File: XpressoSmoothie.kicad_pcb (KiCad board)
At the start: 2 copper layers, 99.7 x 99.7 mm, 116 parts, among them J1 HEADER_4, J10 HEADER_3X2, J11 Pwr_in, J12 HEADER_4, J13 HEADER_4, J14 HEADER_3X2, J15 HEADER_4, J16 HEADER_3, J17 HEADER_3, J18 HEADER_3, J19 HEADER_2, J2 HEADER_4, J20 HEADER_2, J21 HEADER_2, J22 HEADER_2, J23 HEADER_3, J24 HEADER_3, J25 HEADER_3, J26 USB, J27 HEADER_4, J3 HEADER_3, J4 HEADER_3X2, J5 HEADER_3X2, J6 LPCXPRESSO_GENERIC_HEADER, J7 HEADER_4, J8 HEADER_4, J9 HEADER_3X2, M1 LOGO_OSHW, M2 LOGO_OSHW, Q1 IRLB 8743, Q2 IRLB 8743, Q3 IRLB 8743, Q4 IRLB 8743, SW1 SW_PUSH, SW2 SW_PUSH, U1 POLOLU_A4988, U10 TC4422A, U11 TC4422A, U12 LM1117-3.3, U2 POLOLU_A4988, U3 POLOLU_A4988, U4 POLOLU_A4988, U5 POLOLU_A4988, U6 CONN_MICROSD, U7 LM7812CT, U8 TC4422A, U9 TC4422A

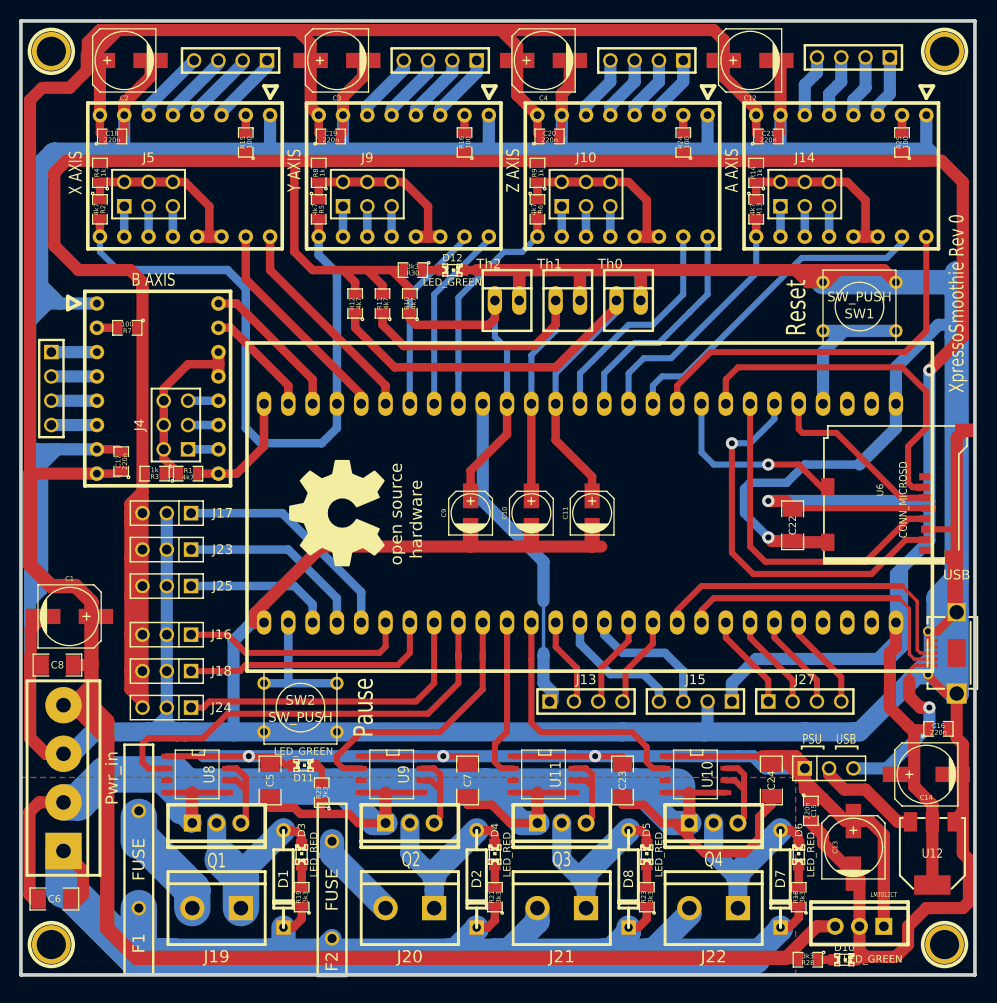
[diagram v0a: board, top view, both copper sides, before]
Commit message: Hid more labels, added some in so that everything is clearly marked and there are no overlaps.
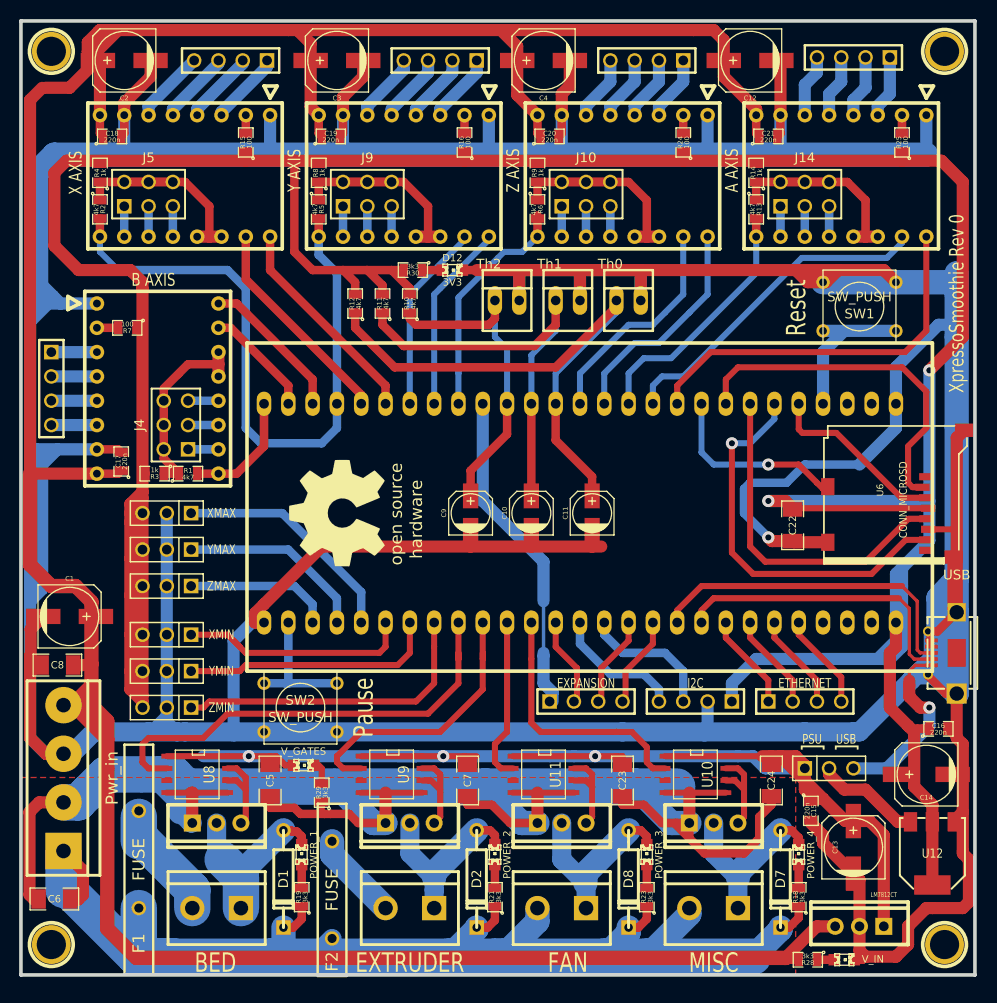
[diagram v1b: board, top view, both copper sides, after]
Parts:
- D10: value LED_GREEN -> V_IN
- D11: value LED_GREEN -> V_GATES
- D12: value LED_GREEN -> 3V3
- D3: value LED_RED -> POWER_1
- D4: value LED_RED -> POWER_2
- D5: value LED_RED -> POWER_3
- D6: value LED_RED -> POWER_4
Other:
- board text added: "BED"
- board text added: "ETHERNET"
- board text added: "EXPANSION"
- board text added: "EXTRUDER"
- board text added: "FAN"
- board text added: "I2C"
- board text added: "MISC"
- board text added: "XMAX"
- board text added: "XMIN"
- board text added: "YMAX"
- board text added: "YMIN"
- board text added: "ZMAX"
- board text added: "ZMIN"
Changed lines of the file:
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@@
     (links 313)
     (no_connects 11)
-    (area 56.388 53.217 179.864657 163.2712)
+    (area 71.564499 53.784499 171.640501 153.860501)
     (thickness 1.6)
-    (drawings 18)
+    (drawings 31)
     (tracks 1095)
     (zones 0)
@@
   )
   (layers
-    (15 F.Cu signal hide)
-    (0 B.Cu signal hide)
+    (15 F.Cu signal)
+    (0 B.Cu signal)
     (16 B.Adhes user)
     (17 F.Adhes user)
     (18 B.Paste user)
     (19 F.Paste user)
-    (20 B.SilkS user hide)
+    (20 B.SilkS user)
     (21 F.SilkS user)
     (22 B.Mask user)
@@
     (descr "Regulateur TO220 serie LM78xx")
     (tags "TR TO220")
-    (fp_text reference Q1 (at 3.937 0 360) (layer F.SilkS)
+    (fp_text reference Q1 (at 3.937 0 360) (layer F.SilkS) hide
       (effects (font (size 1.524 1.016) (thickness 0.2032)))
     )
@@
     (descr "Regulateur TO220 serie LM78xx")
     (tags "TR TO220")
-    (fp_text reference Q2 (at 3.81 -0.127 360) (layer F.SilkS)
+    (fp_text reference Q2 (at 3.81 -0.127 360) (layer F.SilkS) hide
       (effects (font (size 1.524 1.016) (thickness 0.2032)))
     )
@@
     (descr "Regulateur TO220 serie LM78xx")
     (tags "TR TO220")
-    (fp_text reference Q3 (at 3.81 0 360) (layer F.SilkS)
+    (fp_text reference Q3 (at 3.81 0 360) (layer F.SilkS) hide
       (effects (font (size 1.524 1.016) (thickness 0.2032)))
     )
@@
     (descr "Regulateur TO220 serie LM78xx")
     (tags "TR TO220")
-    (fp_text reference Q4 (at 3.81 0 360) (layer F.SilkS)
+    (fp_text reference Q4 (at 3.81 0 360) (layer F.SilkS) hide
       (effects (font (size 1.524 1.016) (thickness 0.2032)))
     )
@@
     (descr "Double rangee de contacts 2 x 5 pins")
     (tags CONN)
-    (fp_text reference J15 (at 0 2.286 180) (layer F.SilkS)
+    (fp_text reference J15 (at 0 2.286 180) (layer F.SilkS) hide
       (effects (font (size 1.016 1.016) (thickness 0.2032)))
     )
@@
     (descr "Connecteur 3 pins")
     (tags "CONN DEV")
-    (fp_text reference J16 (at -5.715 0 180) (layer F.SilkS)
+    (fp_text reference J16 (at -5.715 0 180) (layer F.SilkS) hide
       (effects (font (size 1.016 1.016) (thickness 0.1524)))
     )
@@
     (descr "Connecteur 3 pins")
     (tags "CONN DEV")
-    (fp_text reference J17 (at -5.842 0 180) (layer F.SilkS)
+    (fp_text reference J17 (at -5.842 0 180) (layer F.SilkS) hide
       (effects (font (size 1.016 1.016) (thickness 0.1524)))
     )
@@
     (descr "Connecteur 3 pins")
     (tags "CONN DEV")
-    (fp_text reference J18 (at -5.715 0 180) (layer F.SilkS)
+    (fp_text reference J18 (at -5.715 0 180) (layer F.SilkS) hide
       (effects (font (size 1.016 1.016) (thickness 0.1524)))
     )
@@
     (descr "Connecteur 3 pins")
     (tags "CONN DEV")
-    (fp_text reference J23 (at -5.842 0 180) (layer F.SilkS)
+    (fp_text reference J23 (at -5.842 0 180) (layer F.SilkS) hide
       (effects (font (size 1.016 1.016) (thickness 0.1524)))
     )
@@
     (descr "Connecteur 3 pins")
     (tags "CONN DEV")
-    (fp_text reference J24 (at -5.715 0 180) (layer F.SilkS)
+    (fp_text reference J24 (at -5.715 0 180) (layer F.SilkS) hide
       (effects (font (size 1.016 1.016) (thickness 0.1524)))
     )
@@
     (descr "Connecteur 3 pins")
     (tags "CONN DEV")
-    (fp_text reference J25 (at -5.842 0 180) (layer F.SilkS)
+    (fp_text reference J25 (at -5.842 0 180) (layer F.SilkS) hide
       (effects (font (size 1.016 1.016) (thickness 0.1524)))
     )
@@
     (tags "LED 0805 SMD")
     (attr smd)
-    (fp_text reference D6 (at 2.5654 0.0254 90) (layer F.SilkS)
+    (fp_text reference D6 (at 2.5654 0.0254 90) (layer F.SilkS) hide
       (effects (font (size 0.762 0.762) (thickness 0.127)))
     )
-    (fp_text value LED_RED (at 0 1.27 90) (layer F.SilkS)
+    (fp_text value POWER_4 (at 0 1.27 90) (layer F.SilkS)
       (effects (font (size 0.762 0.762) (thickness 0.127)))
     )
@@
     (tags "LED 0805 SMD")
     (attr smd)
-    (fp_text reference D5 (at 2.6162 -0.0254 90) (layer F.SilkS)
+    (fp_text reference D5 (at 2.6162 -0.0254 90) (layer F.SilkS) hide
       (effects (font (size 0.762 0.762) (thickness 0.127)))
     )
-    (fp_text value LED_RED (at 0 1.27 90) (layer F.SilkS)
+    (fp_text value POWER_3 (at 0 1.27 90) (layer F.SilkS)
       (effects (font (size 0.762 0.762) (thickness 0.127)))
     )
@@
     (tags "LED 0805 SMD")
     (attr smd)
-    (fp_text reference D3 (at 2.5654 0 90) (layer F.SilkS)
+    (fp_text reference D3 (at 2.5654 0 90) (layer F.SilkS) hide
       (effects (font (size 0.762 0.762) (thickness 0.127)))
     )
-    (fp_text value LED_RED (at 0 1.27 90) (layer F.SilkS)
+    (fp_text value POWER_1 (at 0 1.27 90) (layer F.SilkS)
       (effects (font (size 0.762 0.762) (thickness 0.127)))
     )
@@
     (tags "LED 0805 SMD")
     (attr smd)
-    (fp_text reference D4 (at 2.5654 0 90) (layer F.SilkS)
+    (fp_text reference D4 (at 2.5654 0 90) (layer F.SilkS) hide
       (effects (font (size 0.762 0.762) (thickness 0.127)))
     )
-    (fp_text value LED_RED (at 0 1.27 90) (layer F.SilkS)
+    (fp_text value POWER_2 (at 0 1.27 90) (layer F.SilkS)
       (effects (font (size 0.762 0.762) (thickness 0.127)))
     )
@@
     (descr "Bornier d'alimentation 2 pins")
     (tags DEV)
-    (fp_text reference J22 (at 0 -5.08 180) (layer F.SilkS)
+    (fp_text reference J22 (at 0 -5.08 180) (layer F.SilkS) hide
       (effects (font (thickness 0.3048)))
     )
@@
     (descr "Bornier d'alimentation 2 pins")
     (tags DEV)
-    (fp_text reference J19 (at 0 -5.08 180) (layer F.SilkS)
+    (fp_text reference J19 (at 0 -5.08 180) (layer F.SilkS) hide
       (effects (font (thickness 0.3048)))
     )
@@
     (descr "Bornier d'alimentation 2 pins")
     (tags DEV)
-    (fp_text reference J20 (at 0 -5.08 180) (layer F.SilkS)
+    (fp_text reference J20 (at 0 -5.08 180) (layer F.SilkS) hide
       (effects (font (thickness 0.3048)))
     )
@@
     (descr "Bornier d'alimentation 2 pins")
     (tags DEV)
-    (fp_text reference J21 (at 0 -5.08 180) (layer F.SilkS)
+    (fp_text reference J21 (at 0 -5.08 180) (layer F.SilkS) hide
       (effects (font (thickness 0.3048)))
     )
@@
     (tags "LED 0805 SMD")
     (attr smd)
-    (fp_text reference D10 (at 0 -1.27) (layer F.SilkS)
+    (fp_text reference D10 (at 0 -1.27) (layer F.SilkS) hide
       (effects (font (size 0.762 0.762) (thickness 0.127)))
     )
-    (fp_text value LED_GREEN (at 2.9845 -0.0635) (layer F.SilkS)
+    (fp_text value V_IN (at 2.9845 -0.0635) (layer F.SilkS)
       (effects (font (size 0.762 0.762) (thickness 0.127)))
     )
@@
     (tags "LED 0805 SMD")
     (attr smd)
-    (fp_text reference D11 (at 0 1.3335) (layer F.SilkS)
+    (fp_text reference D11 (at 0 1.3335) (layer F.SilkS) hide
       (effects (font (size 0.762 0.762) (thickness 0.127)))
     )
-    (fp_text value LED_GREEN (at 0 -1.4605) (layer F.SilkS)
+    (fp_text value V_GATES (at 0 -1.4605) (layer F.SilkS)
       (effects (font (size 0.762 0.762) (thickness 0.127)))
     )
@@
       (effects (font (size 0.762 0.762) (thickness 0.127)))
     )
-    (fp_text value LED_GREEN (at 0 1.27) (layer F.SilkS)
+    (fp_text value 3V3 (at 0 1.27) (layer F.SilkS)
       (effects (font (size 0.762 0.762) (thickness 0.127)))
     )
@@
     (descr "Double rangee de contacts 2 x 5 pins")
     (tags CONN)
-    (fp_text reference J13 (at 0 -2.286) (layer F.SilkS)
+    (fp_text reference J13 (at 0 -2.286) (layer F.SilkS) hide
       (effects (font (size 1.016 1.016) (thickness 0.2032)))
     )
@@
     (descr "Double rangee de contacts 2 x 5 pins")
     (tags CONN)
-    (fp_text reference J27 (at 0 -2.286) (layer F.SilkS)
+    (fp_text reference J27 (at 0 -2.286) (layer F.SilkS) hide
       (effects (font (size 1.016 1.016) (thickness 0.2032)))
     )
@@
       (xy -3.37312 4.99872)) (layer F.SilkS) (width 0.00254))
   )
+  (gr_text MISC (at 144.145 152.4) (layer F.SilkS)
+    (effects (font (size 2.032 1.524) (thickness 0.3048)))
+  )
+  (gr_text FAN (at 128.905 152.4) (layer F.SilkS)
+    (effects (font (size 2.032 1.524) (thickness 0.3048)))
+  )
+  (gr_text EXTRUDER (at 112.395 152.4) (layer F.SilkS)
+    (effects (font (size 2.032 1.524) (thickness 0.3048)))
+  )
+  (gr_text BED (at 92.075 152.4) (layer F.SilkS)
+    (effects (font (size 2.032 1.524) (thickness 0.3048)))
+  )
+  (gr_text ETHERNET (at 153.67 123.19) (layer F.SilkS)
+    (effects (font (size 1.016 0.762) (thickness 0.1524)))
+  )
+  (gr_text I2C (at 142.24 123.19) (layer F.SilkS)
+    (effects (font (size 1.016 0.762) (thickness 0.1524)))
+  )
+  (gr_text EXPANSION (at 130.81 123.19) (layer F.SilkS)
+    (effects (font (size 1.016 0.762) (thickness 0.1524)))
+  )
+  (gr_text ZMIN (at 92.71 125.73) (layer F.SilkS)
+    (effects (font (size 1.016 0.762) (thickness 0.1524)))
+  )
+  (gr_text YMIN (at 92.71 121.92) (layer F.SilkS)
+    (effects (font (size 1.016 0.762) (thickness 0.1524)))
+  )
+  (gr_text XMIN (at 92.71 118.11) (layer F.SilkS)
+    (effects (font (size 1.016 0.762) (thickness 0.1524)))
+  )
+  (gr_text ZMAX (at 92.71 113.03) (layer F.SilkS)
+    (effects (font (size 1.016 0.762) (thickness 0.1524)))
+  )
+  (gr_text YMAX (at 92.71 109.22) (layer F.SilkS)
+    (effects (font (size 1.016 0.762) (thickness 0.1524)))
+  )
+  (gr_text XMAX (at 92.71 105.41) (layer F.SilkS)
+    (effects (font (size 1.016 0.762) (thickness 0.1524)))
+  )
   (gr_text "B AXIS" (at 85.598 81.026) (layer F.SilkS)

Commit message: Adjusted clearance for pads/vias/tracks to 0.2 mm. Still within allowed tolerances for Seeedstudio (and probably other fab houses), but stops the DRC from complaining.
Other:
- net class Default: clearance 0.25 -> 0.2
- rule trace_clearance: 0.25 -> 0.2
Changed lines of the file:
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@@
     (links 313)
     (no_connects 11)
-    (area 71.564499 53.784499 171.640501 153.860501)
+    (area 56.388 53.217 179.864657 163.2712)
     (thickness 1.6)
     (drawings 31)
@@
     (18 B.Paste user)
     (19 F.Paste user)
-    (20 B.SilkS user)
+    (20 B.SilkS user hide)
     (21 F.SilkS user)
     (22 B.Mask user)
@@
     (user_trace_width 3)
     (user_trace_width 3.81)
-    (trace_clearance 0.25)
+    (trace_clearance 0.2)
     (zone_clearance 0.508)
     (zone_45_only yes)
@@
   (net 131 ZMIN)
   (net_class Default "This is the default net class."
-    (clearance 0.25)
+    (clearance 0.2)
     (trace_width 0.635)
     (via_dia 1.27)

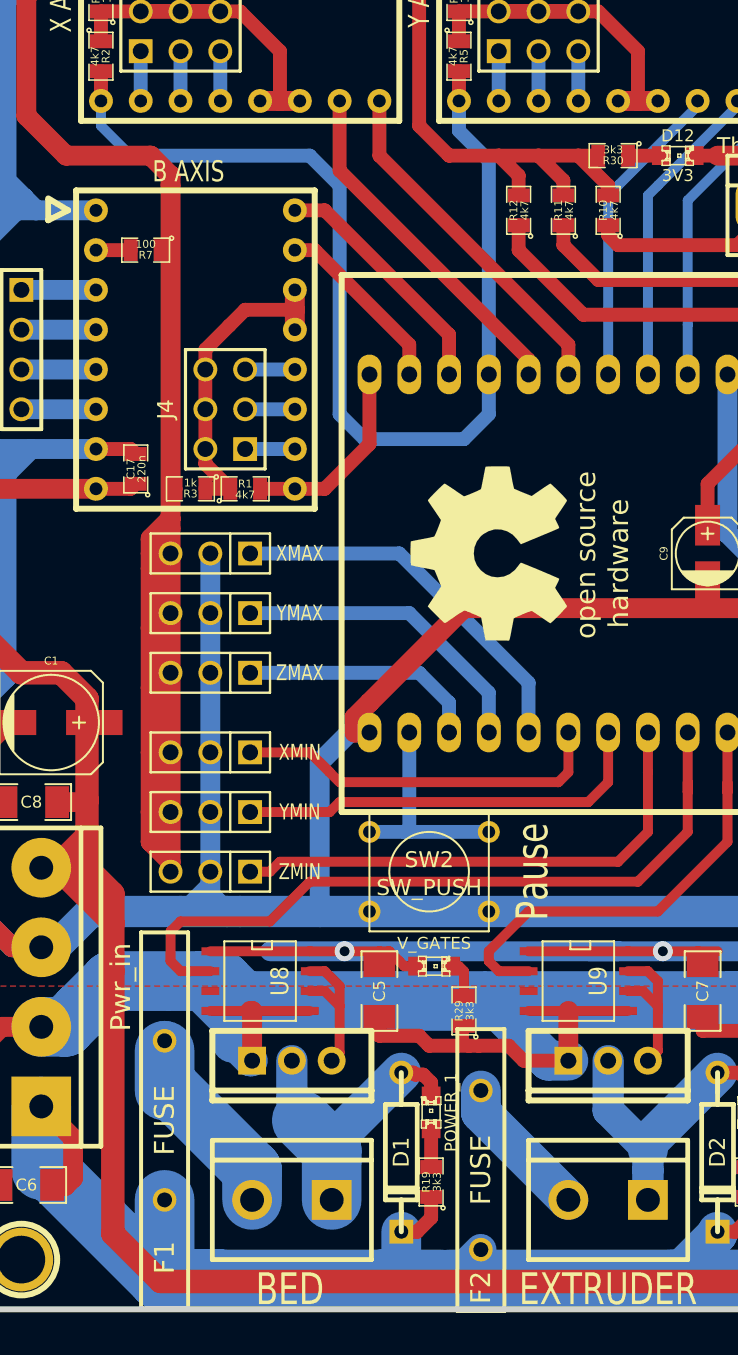
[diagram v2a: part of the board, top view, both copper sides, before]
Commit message: minor xy-en reroute
minor xy-en reroute
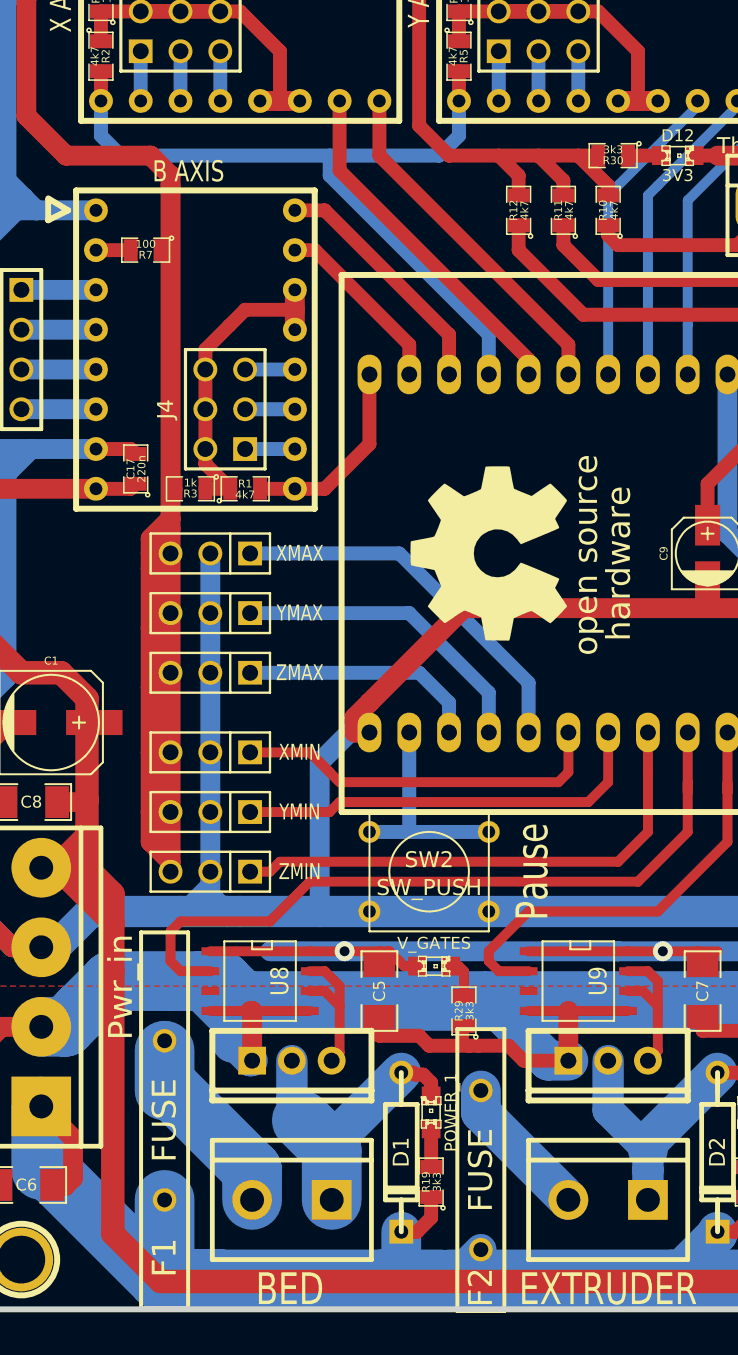
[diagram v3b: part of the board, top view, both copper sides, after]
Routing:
- net X-EN: track 68.5 -> 50.3 mm
